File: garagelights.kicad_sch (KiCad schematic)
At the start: 23 parts, among them J1 Conn_01x04, J3 +V, J4 GND, U1 NE555P, U2 NE555P, U3 4013, U4 NE556

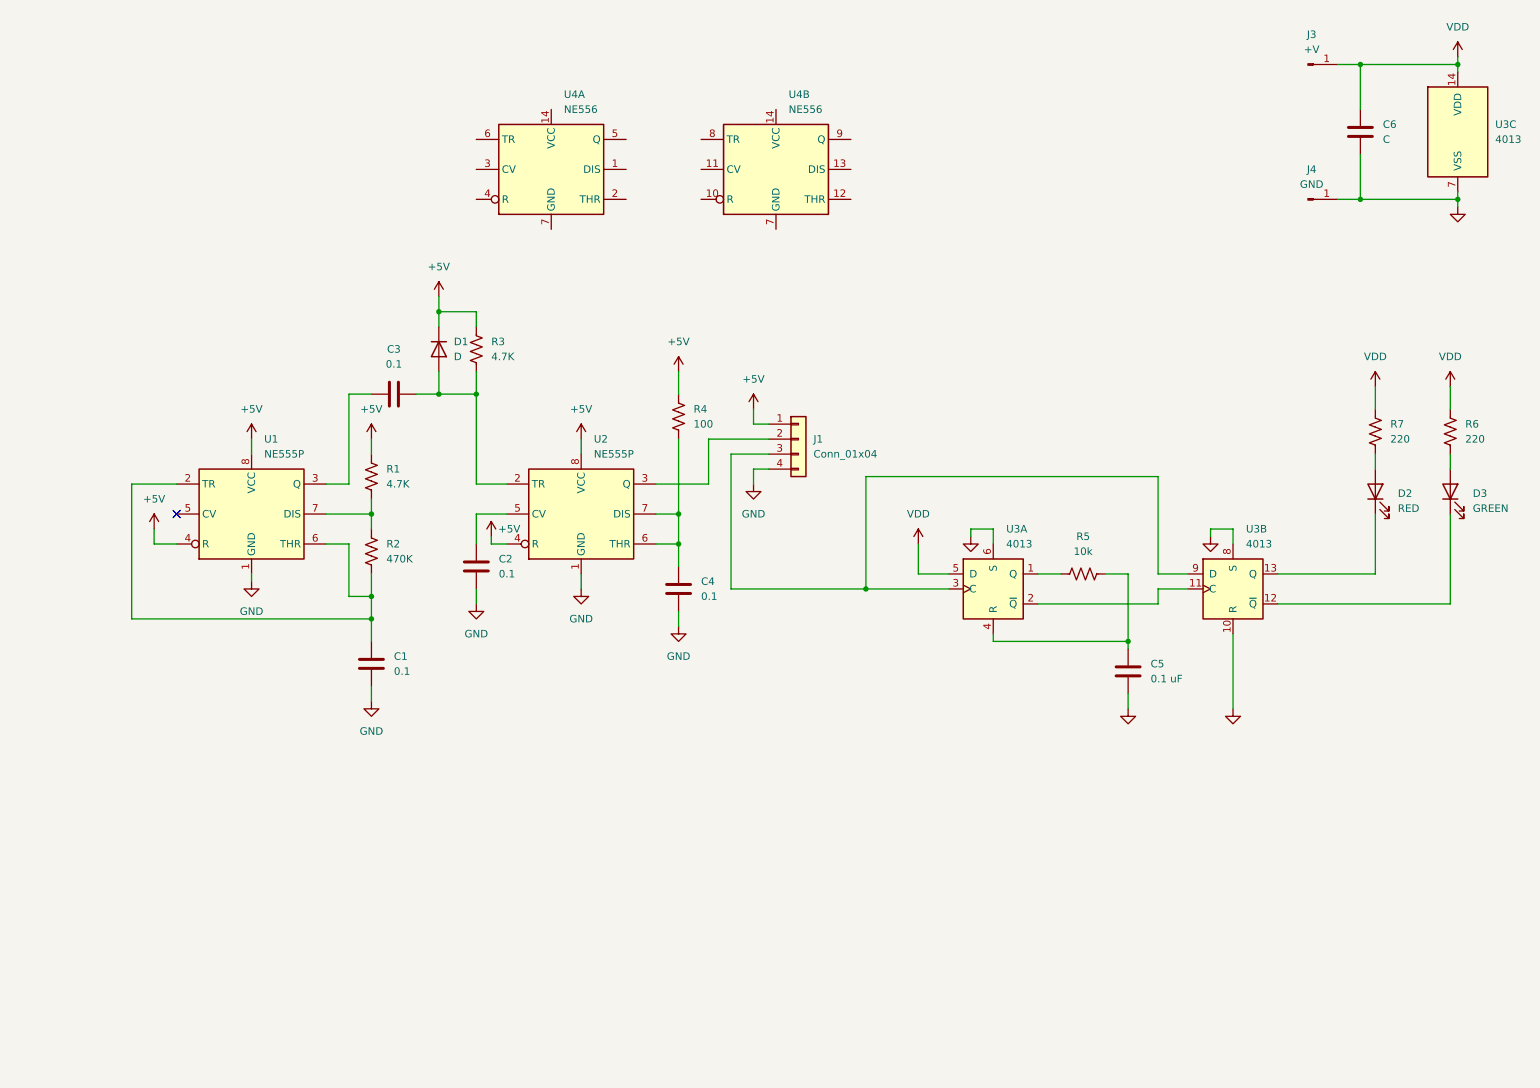
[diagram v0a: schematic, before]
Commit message: Added FETs and yellow light
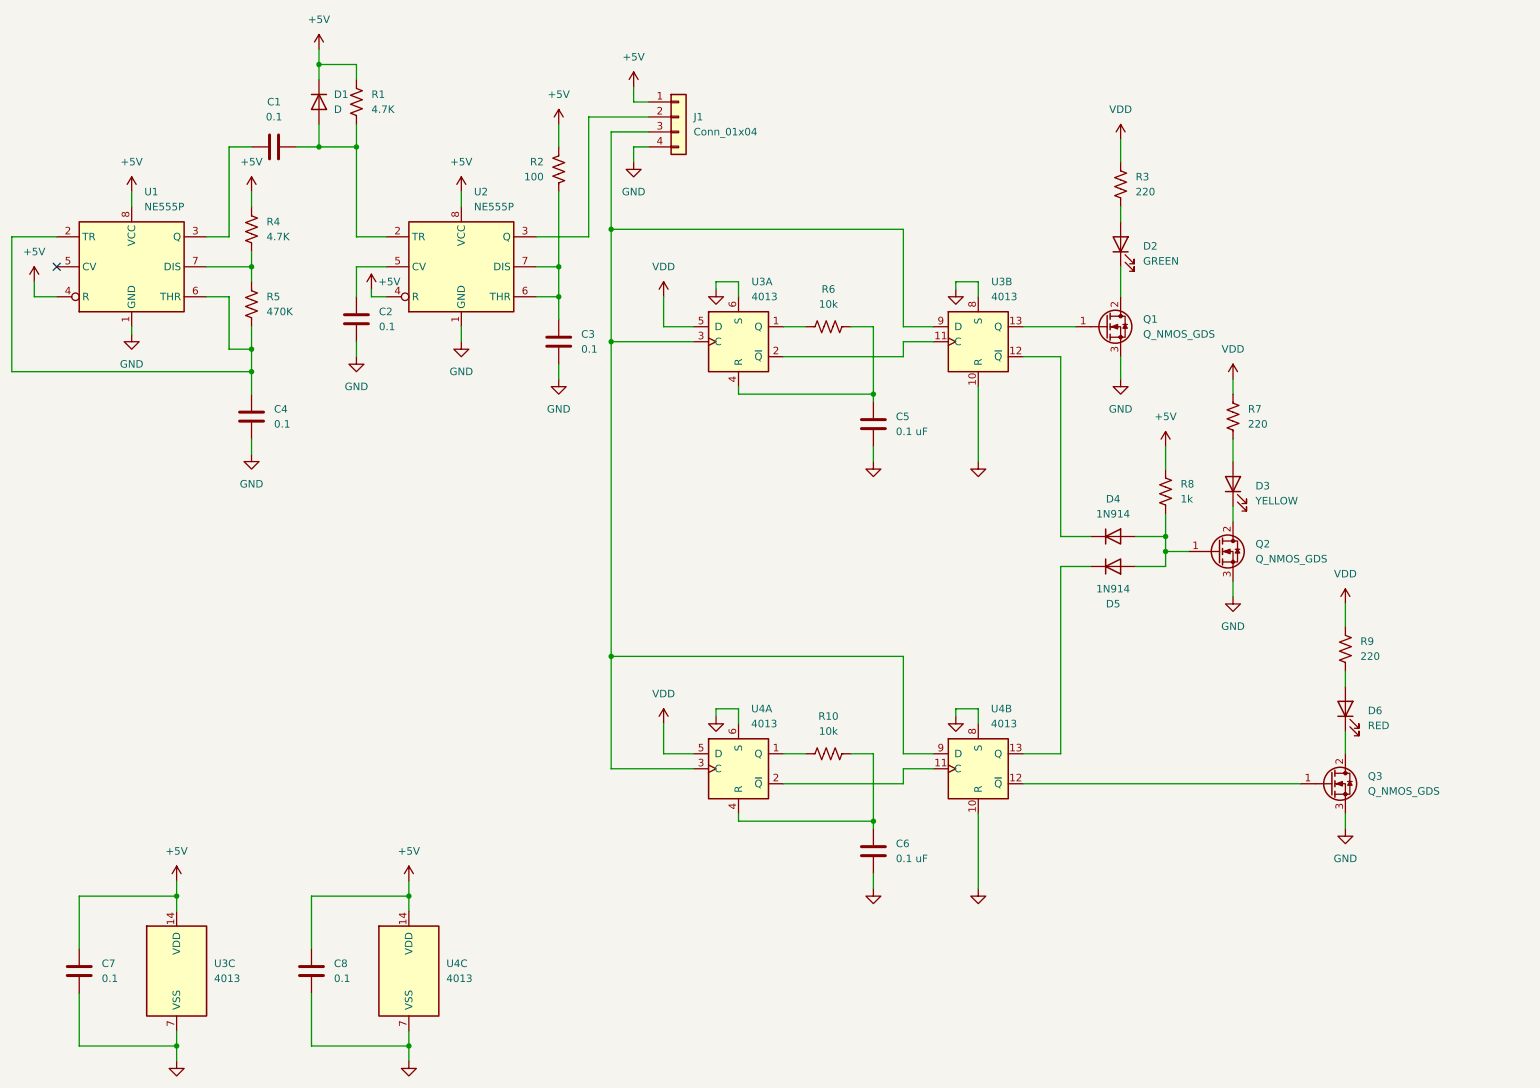
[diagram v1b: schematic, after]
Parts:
- removed J3: +V, symbol Connector:Conn_01x01_Pin
- removed J4: GND, symbol Connector:Conn_01x01_Pin
- removed R6: 220, symbol Device:R_US
- removed U4: NE556, symbol Timer:NE556
- added C6: 0.1 uF, symbol Device:C
- added C8: 0.1, symbol Device:C
- added D4, D5: 1N914, Diode_THT:D_DO-35_SOD27_P7.62mm_Horizontal, symbol Diode:1N914
- added D6: RED, symbol Device:LED
- added Q1, Q2, Q3: Q_NMOS_GDS, symbol Transistor_FET:Q_NMOS_GDS
- added R10: 10k, symbol Device:R_US
- added R7, R9: 220, symbol Device:R_US
- added R8: 1k, symbol Device:R_US
- added U4: 4013, symbol 4xxx:4013
- C7: renamed from C6; value C -> 0.1
- D2: value RED -> GREEN
- D3: value GREEN -> YELLOW
- renumbered C3 to C1, C4 to C3, C1 to C4, R3 to R1, R4 to R2, R7 to R3, R1 to R4, R2 to R5, R5 to R6
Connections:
- net +5V: now also C7.1, U3.14 (VDD), C8.1, R8.1, U4.14 (VDD)
- net GND: now also C6.2, C8.2, Q1.3 (S), Q2.3 (S), Q3.3 (S), U4.10 (R), U4.6 (S), U4.7 (VSS), U4.8 (S)
- net VDD: now also R7.1, R9.1, U4.5 (D); no longer C7.1, U3.14 (VDD)
- net at D3.1 (K): now also Q2.2 (D); no longer U3.12 (~{Q})
- net at D3.2 (A): now also R7.2
- net at J1.3 (Pin_3), U3.3 (C), U3.9 (D): now also U4.3 (C), U4.9 (D)
- net at U3.13 (Q): now also Q1.1 (G); no longer D2.1 (K)
- new net: R10.1, U4.1 (Q)
- new net: C6.1, R10.2, U4.4 (R)
- new net: D5.1 (K), U4.13 (Q)
- new net: D4.2 (A), D5.2 (A), Q2.1 (G), R8.2
- new net: Q3.1 (G), U4.12 (~{Q})
- new net: D6.1 (K), Q3.2 (D)
- new net: D6.2 (A), R9.2
- new net: U4.11 (C), U4.2 (~{Q})
- new net: D2.1 (K), Q1.2 (D)
- new net: D4.1 (K), U3.12 (~{Q})
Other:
- moved on the sheet: C1, C2, C3, C4, C5, C7, D1, D2, D3, J1, R1, R2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

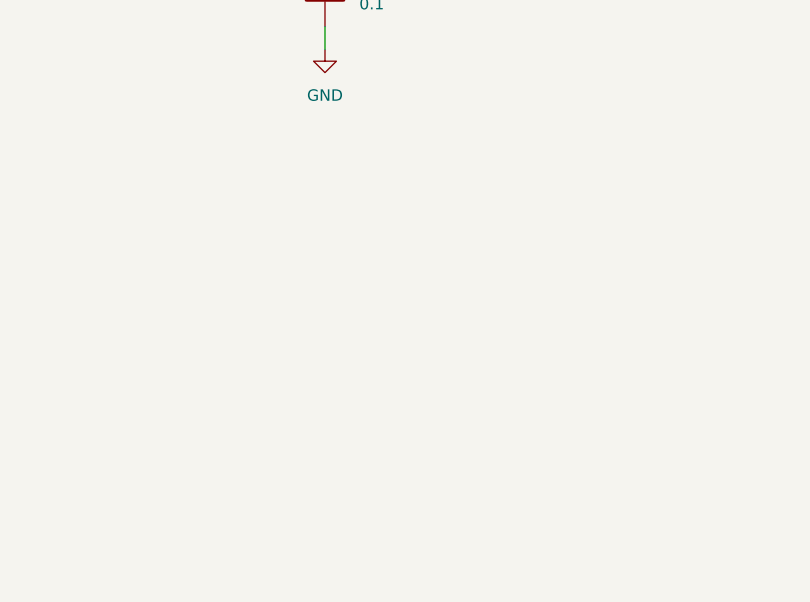
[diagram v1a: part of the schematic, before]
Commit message: Working towards debouncing.
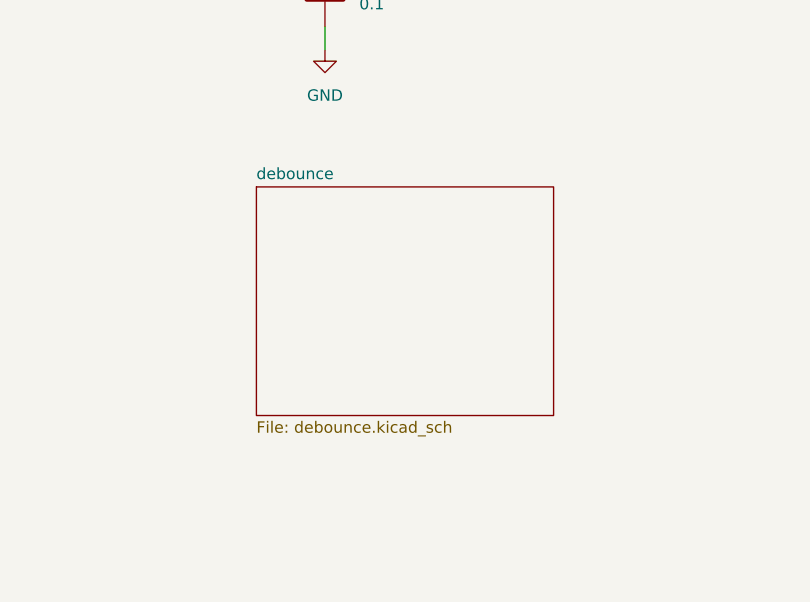
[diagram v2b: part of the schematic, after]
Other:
- added sheet debounce (debounce.kicad_sch)
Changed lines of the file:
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@@
+		)
+	)
+	(sheet
+		(at 55.88 105.41)
+		(size 33.02 25.4)
+		(exclude_from_sim no)
+		(in_bom yes)
+		(on_board yes)
+		(dnp no)
+		(fields_autoplaced yes)
+		(stroke
+			(width 0.1524)
+			(type solid)
+		)
+		(fill
+			(color 0 0 0 0.0000)
+		)
+		(property "Sheetname" "debounce"
+			(at 55.88 104.6984 0)
+			(effects
+				(font
+					(size 1.27 1.27)
+				)
+				(justify left bottom)
+			)
+		)
+		(property "Sheetfile" "debounce.kicad_sch"
+			(at 55.88 131.3946 0)
+			(effects
+				(font
+					(size 1.27 1.27)
+				)
+				(justify left top)
+			)
+		)
+		(instances
+			(project "garagelights"
+				(path "/8304b3b7-1ae3-4935-a8ef-a9ab1b0a3004"
+					(page "2")
+				)
+			)
 		)
 	)

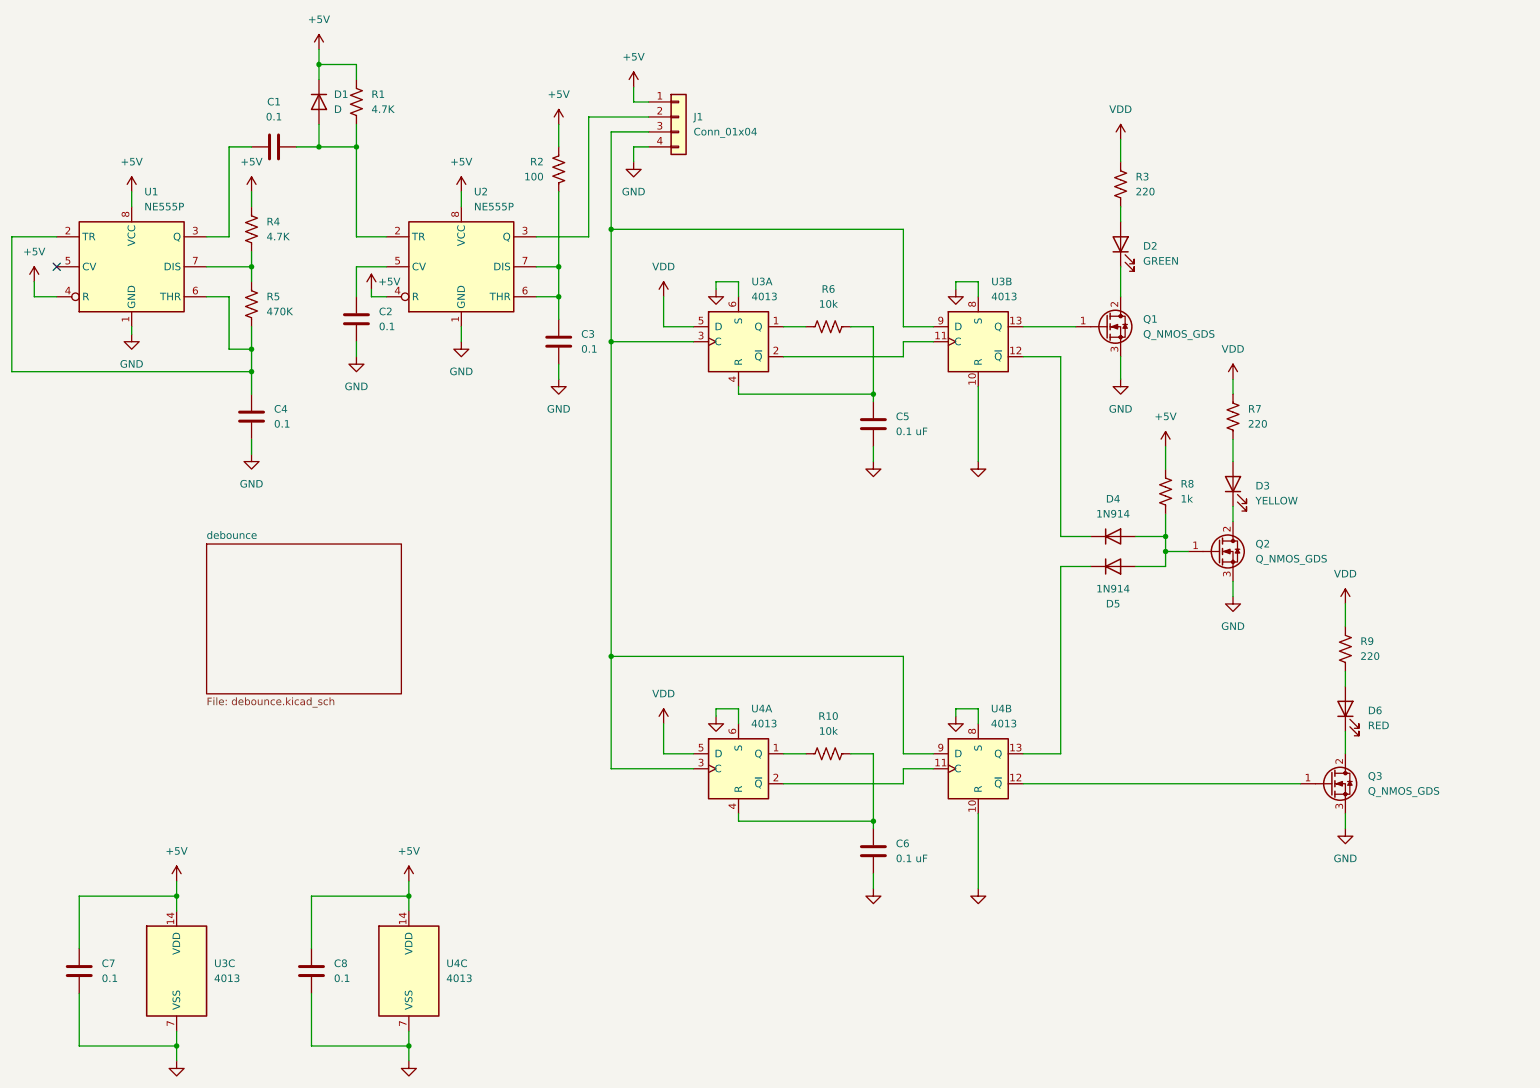
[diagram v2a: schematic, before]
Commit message: More hierarchical; adding debounce
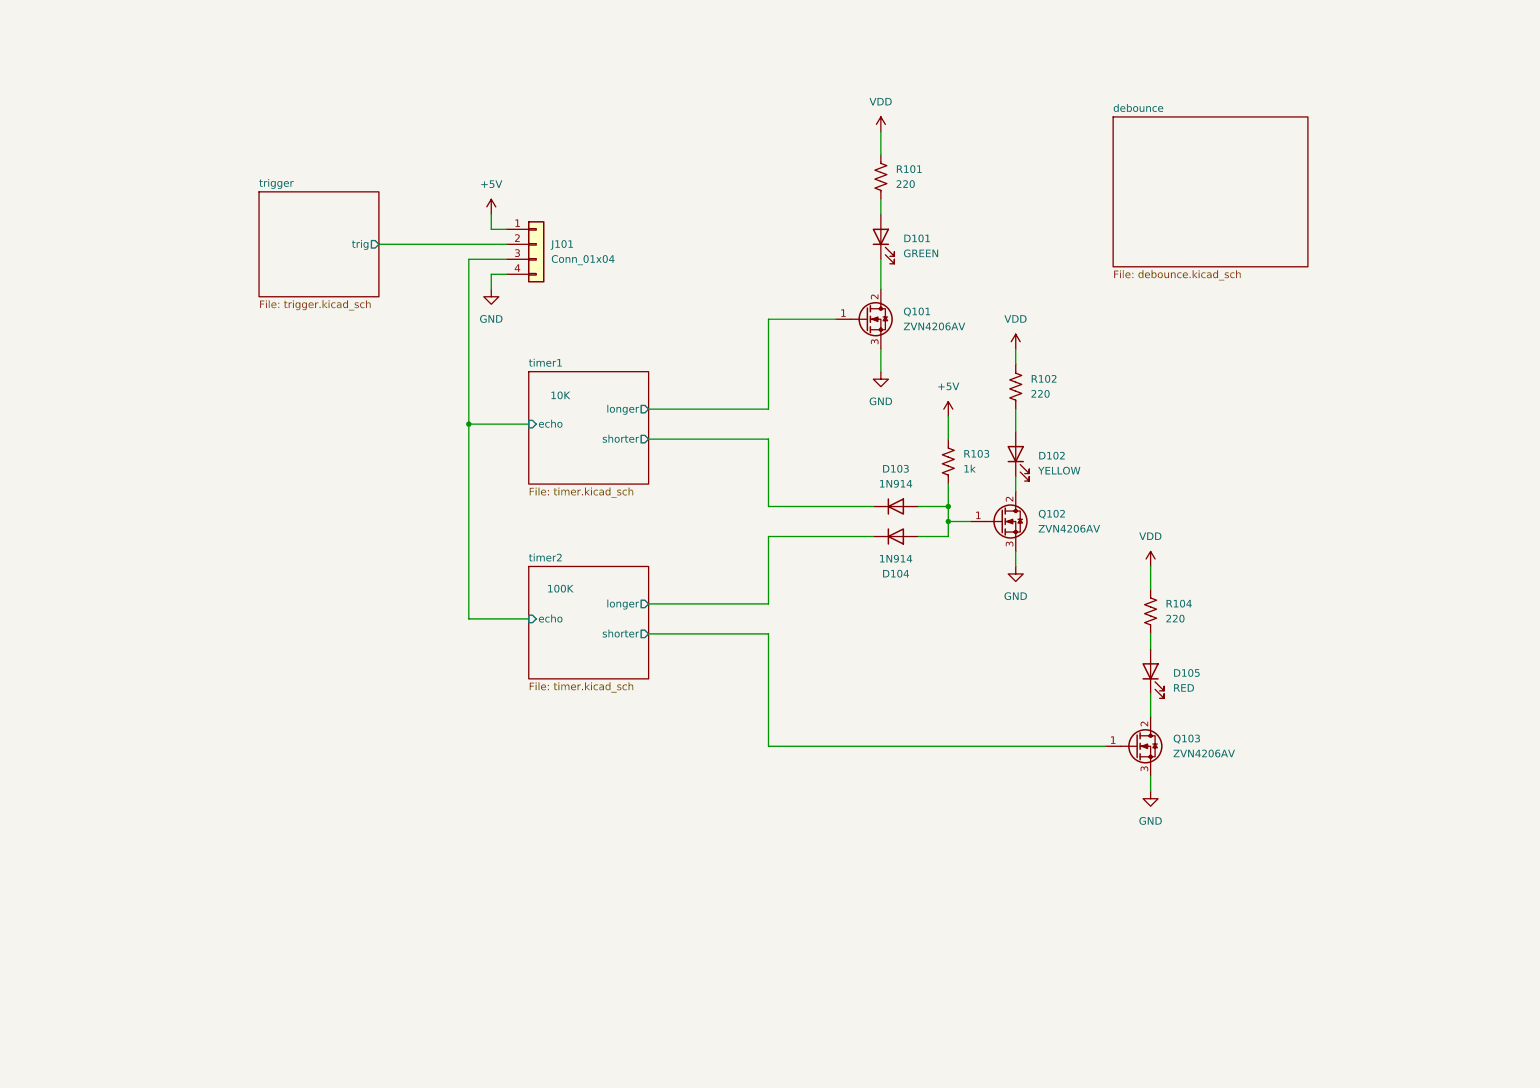
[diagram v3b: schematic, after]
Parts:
- removed C1, C2, C3, C4, C7, C8: 0.1, symbol Device:C
- removed C5, C6: 0.1 uF, symbol Device:C
- removed D1: D, symbol Device:D
- removed R1, R4: 4.7K, symbol Device:R_US
- removed R10, R6: 10k, symbol Device:R_US
- removed R2: 100, symbol Device:R_US
- removed R5: 470K, symbol Device:R_US
- removed U1, U2: NE555P, Package_DIP:DIP-8_W7.62mm, symbol Timer:NE555P
- removed U3, U4: 4013, symbol 4xxx:4013
- Q101: renamed from Q1; value Q_NMOS_GDS -> ZVN4206AV
- Q102: renamed from Q2; value Q_NMOS_GDS -> ZVN4206AV
- Q103: renamed from Q3; value Q_NMOS_GDS -> ZVN4206AV
- renumbered D2 to D101, D3 to D102, D4 to D103, D5 to D104, D6 to D105, J1 to J101, R3 to R101, R7 to R102, R8 to R103, R9 to R104
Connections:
- net timer2/longer: now reaches D104.1 (K)
- net timer2/shorter: now reaches Q103.1 (G)
- net timer1/echo: now reaches J101.3 (Pin_3)
- net trigger/trig: now reaches J101.2 (Pin_2)
- net timer1/longer: now reaches Q101.1 (G)
- net timer1/shorter: now reaches D103.1 (K)
- no-connect marks 1 -> 0
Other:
- added sheet timer1 (timer.kicad_sch)
- added sheet timer2 (timer.kicad_sch)
- added sheet trigger (trigger.kicad_sch)
- moved on the sheet: D101, D102, D103, D104, D105, J101, Q101, Q102, Q103, R101, R102, R103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

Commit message: prettify
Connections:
- net timer1/echo renamed echo
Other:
- moved on the sheet: D101, D105, Q101, Q103, R101, R104
